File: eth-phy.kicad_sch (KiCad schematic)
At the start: 60 parts, among them J2 JST_SH_1x12_SM12B-SRSS-TB-LF-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, U7 RTL8211FDI-CG, U8 TPD4E05U06QDQARQ1, U9 TPD4E05U06QDQARQ1, Y2 Resonator_25MHz_445

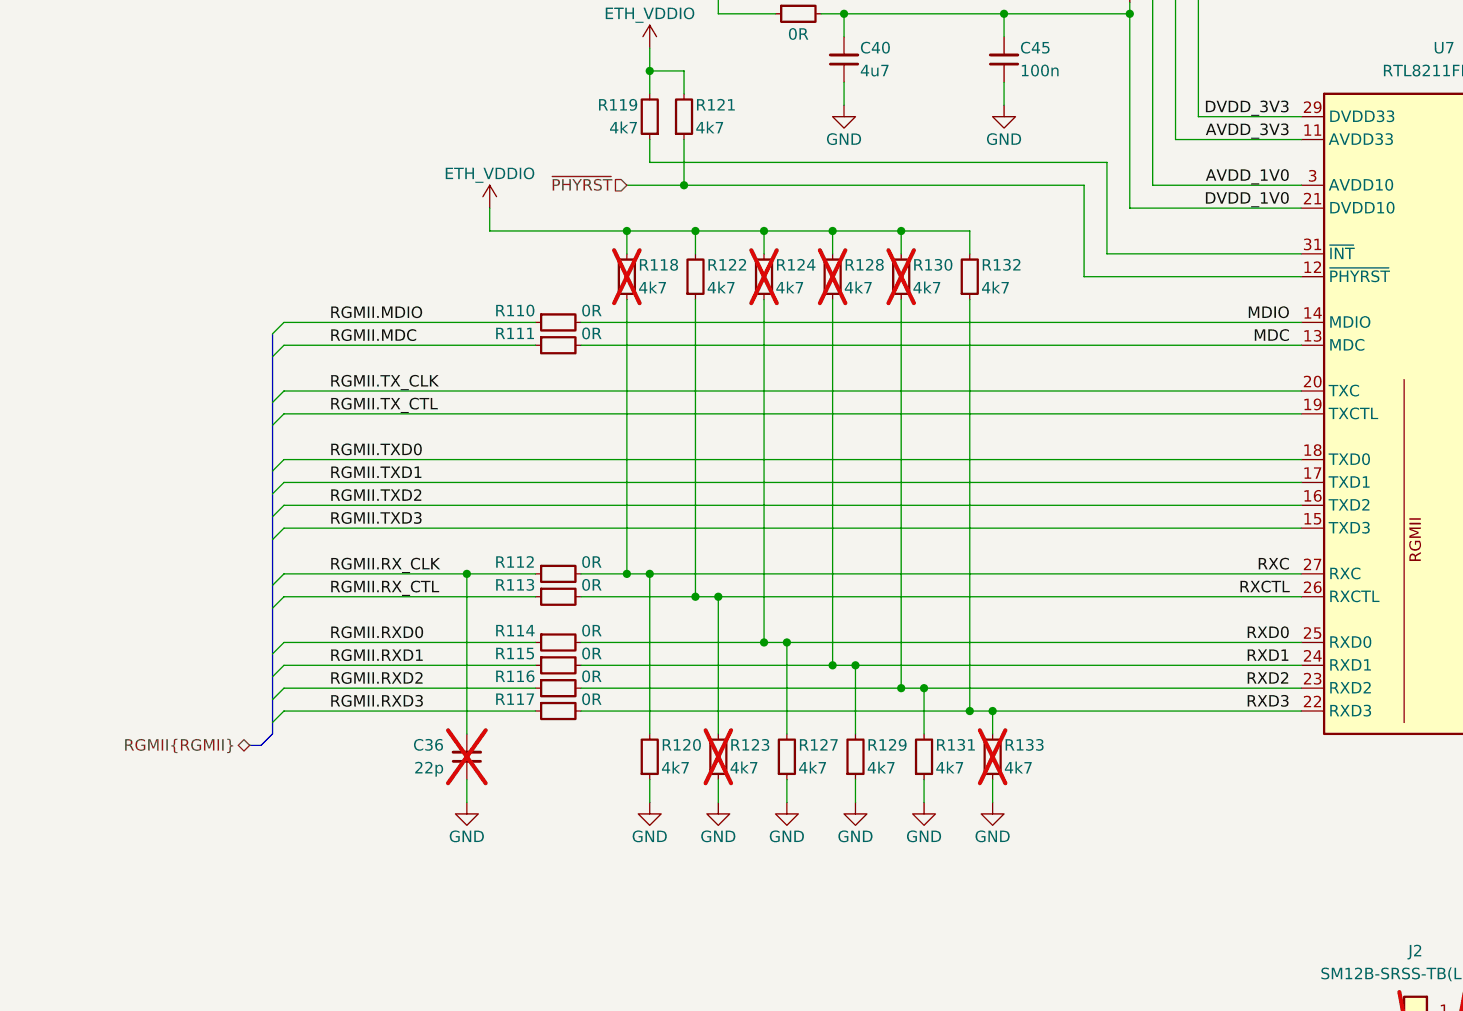
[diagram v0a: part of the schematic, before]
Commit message: [#83767] Add MDIO pullup
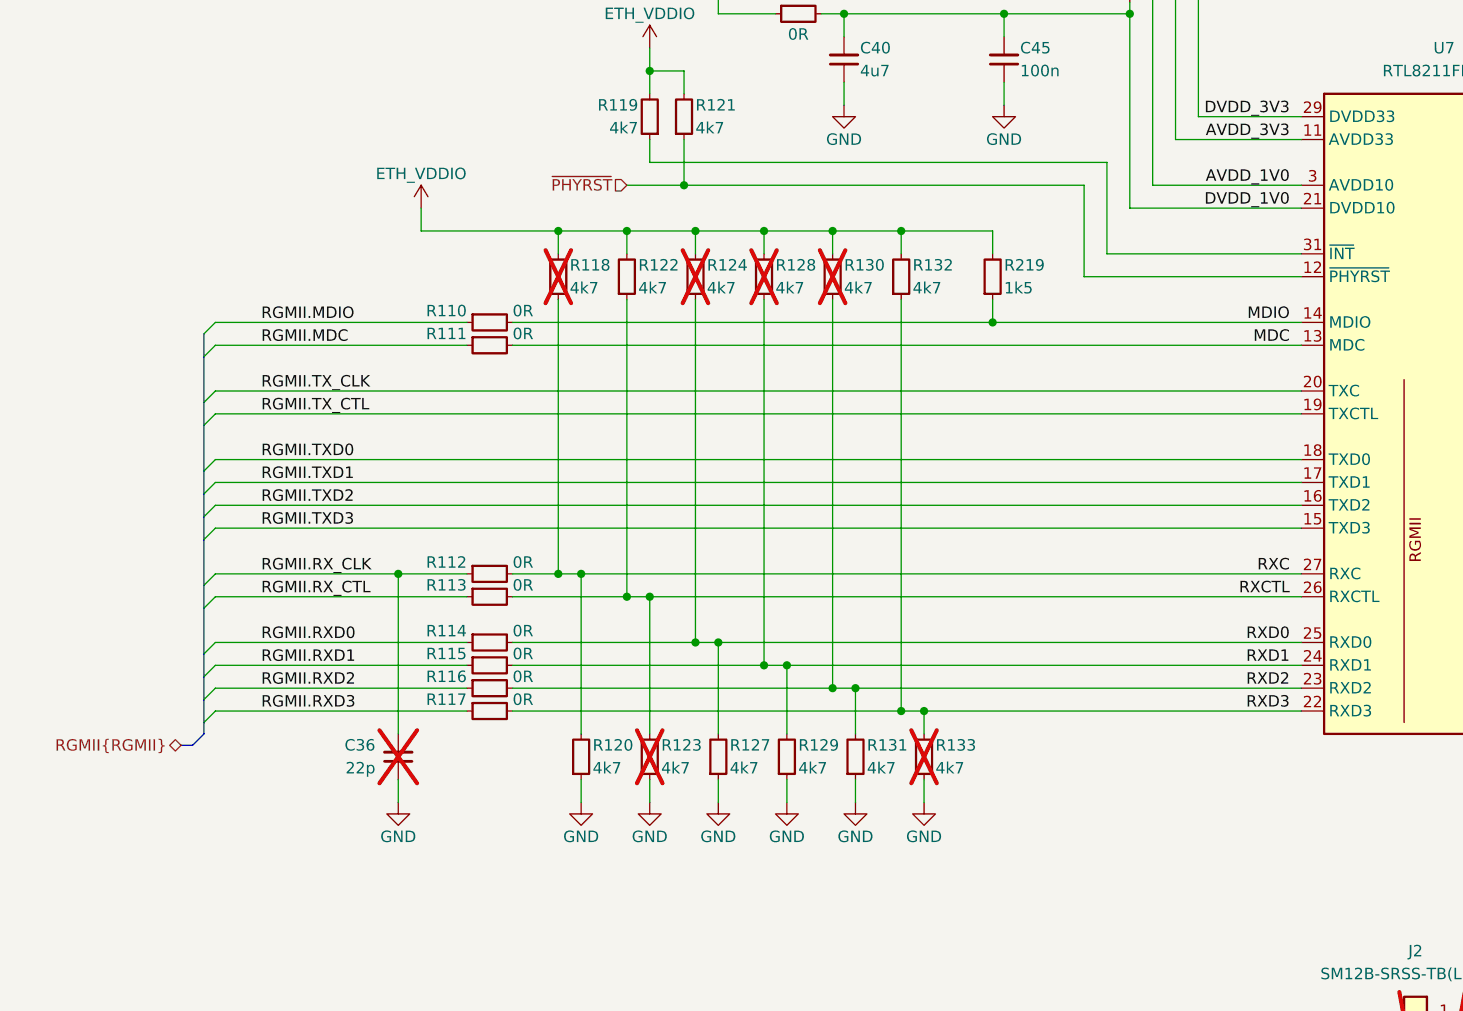
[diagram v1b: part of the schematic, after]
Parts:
- added R219: R_1k5_0402, antmicro-footprints:R_0402_1005Metric, symbol antmicroResistors0402:R_1k5_0402
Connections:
- net ETH_VDDIO: now also R219.2
- net MDIO: now also R219.1
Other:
- moved on the sheet: C36, R110, R111, R112, R113, R114, R115, R116, R117, R118, R120, R122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

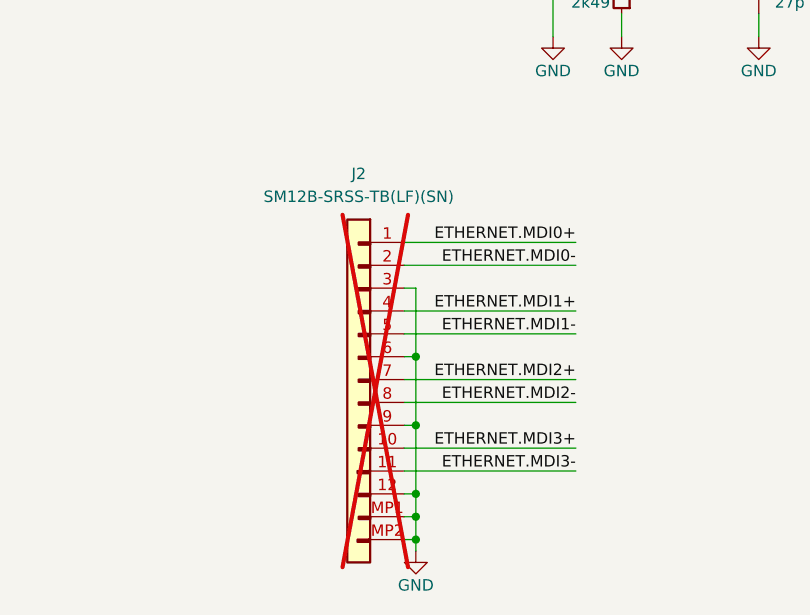
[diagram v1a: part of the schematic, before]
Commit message: [#83767] Remove FFC Eth connector
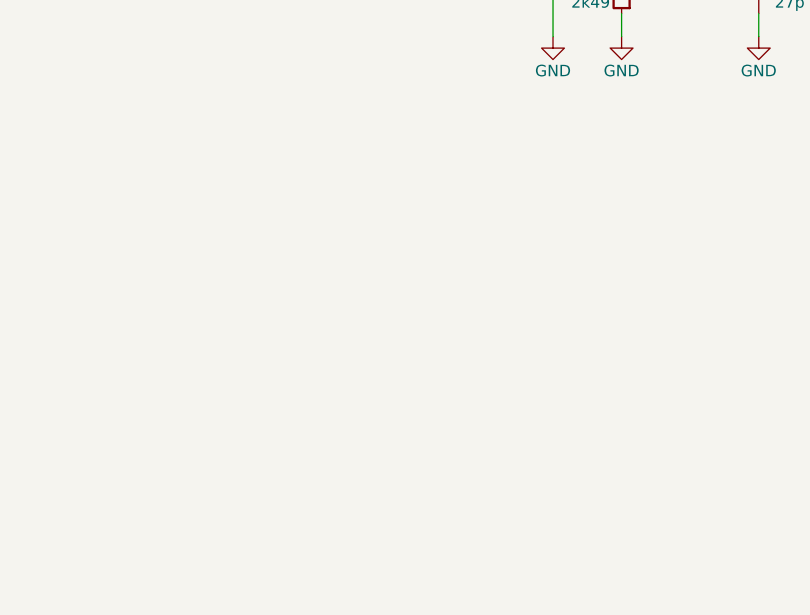
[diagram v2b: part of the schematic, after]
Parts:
- removed J2: JST_SH_1x12_SM12B-SRSS-TB-LF-SN, antmicro-footprints:Conn_JST_SH_1x12_SM12B-SRSS-TB-LF-SN, symbol antmicroWire2BoardConnectors:JST_SH_1x12_SM12B-SRSS-TB-LF-SN

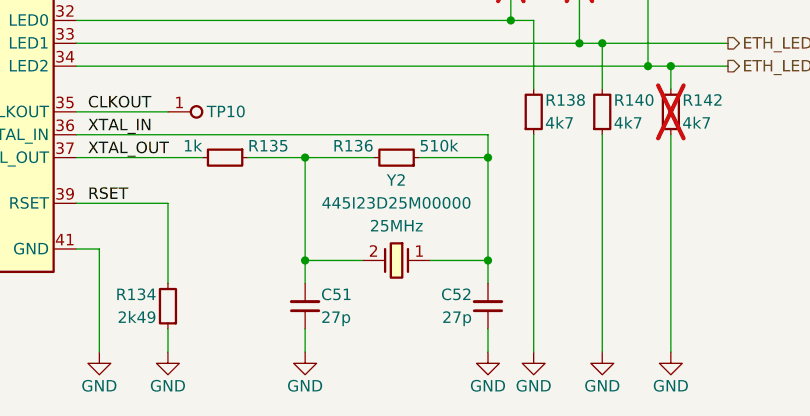
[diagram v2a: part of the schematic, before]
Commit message: [#83767] Replace RTL8211FDI-CG oscillator
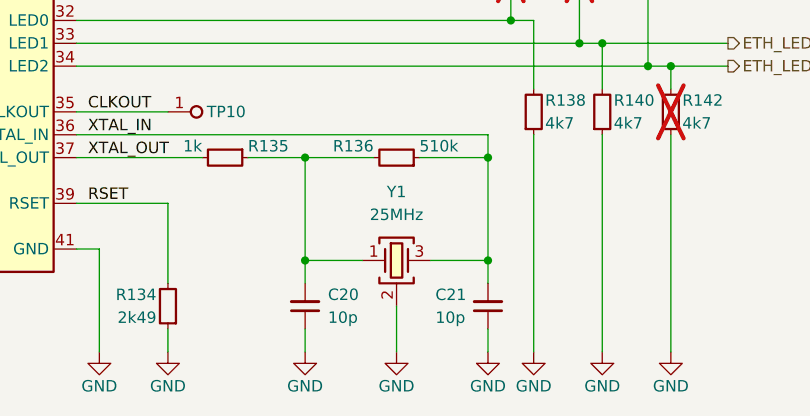
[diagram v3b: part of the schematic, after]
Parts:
- removed C51, C52: C_27p_0402, antmicro-footprints:C_0402_1005Metric, symbol antmicroCapacitors0402:C_27p_0402
- removed Y2: Resonator_25MHz_445, antmicro-footprints:Resonator_SMD_CTS_445_5x3.2mm, symbol antmicroResonators:Resonator_25MHz_445
- added C20, C21: C_10p_25V_0402, antmicro-footprints:C_0402_1005Metric, symbol antmicroCapacitors0402:C_10p_25V_0402
- added Y1: Resonator_25MHz_XRCGB, antmicro-footprints:Resonator_SMD_Murata_XRCGB_2x1.6x0.65mm, symbol antmicroResonators:Resonator_25MHz_XRCGB
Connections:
- net GND: now also C20.1, C21.1, Y1.2 (SH), Y1.4 (SH)
- net XTAL_IN: now also C21.2, Y1.3
- net at R135.1, R136.2: now also C20.2, Y1.1
